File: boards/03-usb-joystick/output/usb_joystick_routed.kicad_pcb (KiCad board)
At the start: 2 copper layers, 80 x 60 mm, 19 parts, among them J1 USB-C, J2 Joystick, SW1 Button, SW2 Button, SW3 Button, SW4 Button, U1 MCU, Y1 16MHz

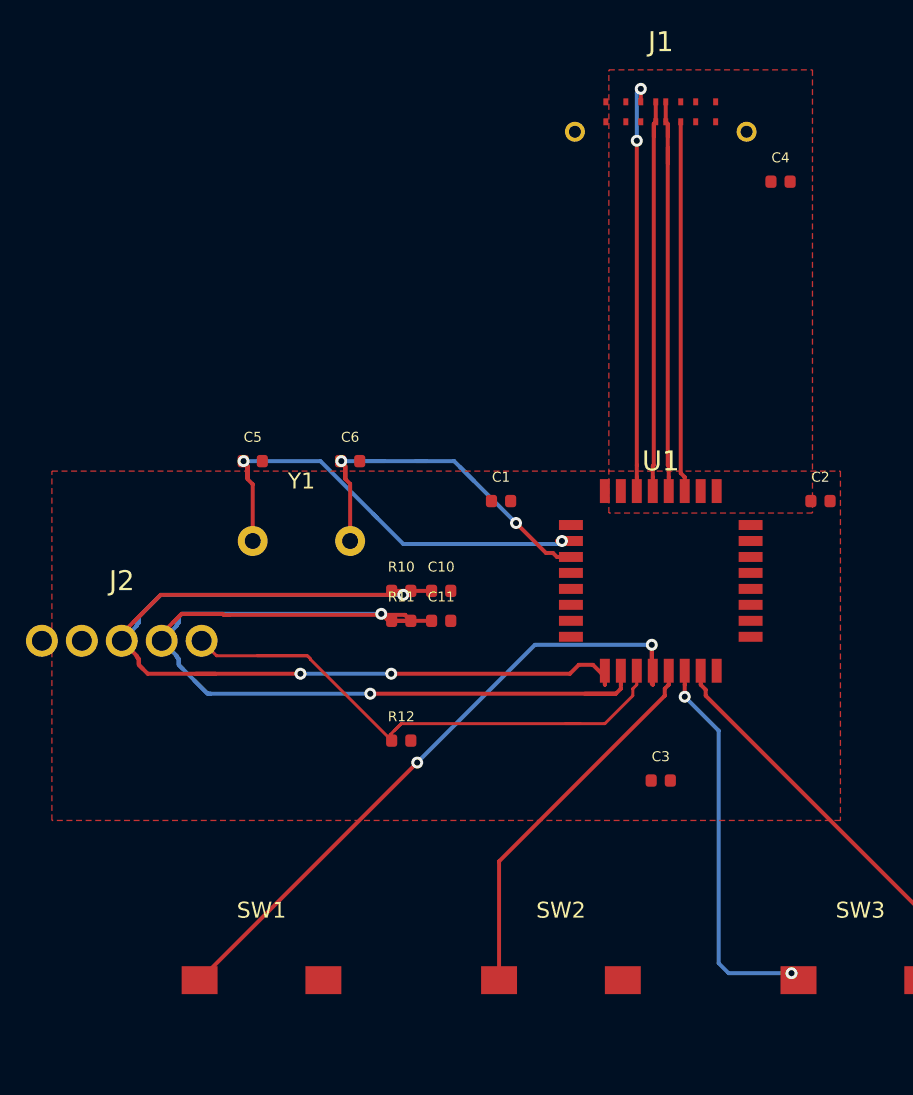
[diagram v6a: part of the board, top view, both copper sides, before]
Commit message: fix(boards/03): restore refill-only routed PCB from bundle — undo in-place re-route clobber
The committed usb_joystick_routed.kicad_pcb at the previous head was a
re-clobbered re-route (570 segments, 257/245 multiset diff vs main) — an
in-place test/demo run overwrote the artifact AFTER the correct refill
(same failure class as issue #3580). The correct refill-only artifact
survived inside manufacturing/kicad_project.zip; this commit restores the
standalone file from that zip (now byte-identical to the bundle-embedded
PCB, sha256 b793b9b4).

Independently re-verified vs origin/main:
- 582 segments, (start,end,width,layer,net) multiset identical (0/0 diff)
- 15 vias identical, 19 footprints, 4 zone outlines unchanged
- filled_polygon data is the only substantive diff (7/10 polygons regenerated)
- kct check --mfr jlcpcb-tier1 --only segment_zone --errors-only: 0
- full kct check --mfr jlcpcb-tier1: 0 errors / 16 warnings
- scripts/ci/check_routed_drc.py strict gate: OK — 0 errors

No bundle changes needed: kicad_project.zip sha256 already matches
manifest.json (32827137…, 83827 bytes).

Co-Authored-By: Claude Opus 4.7 <noreply@anthropic.com>
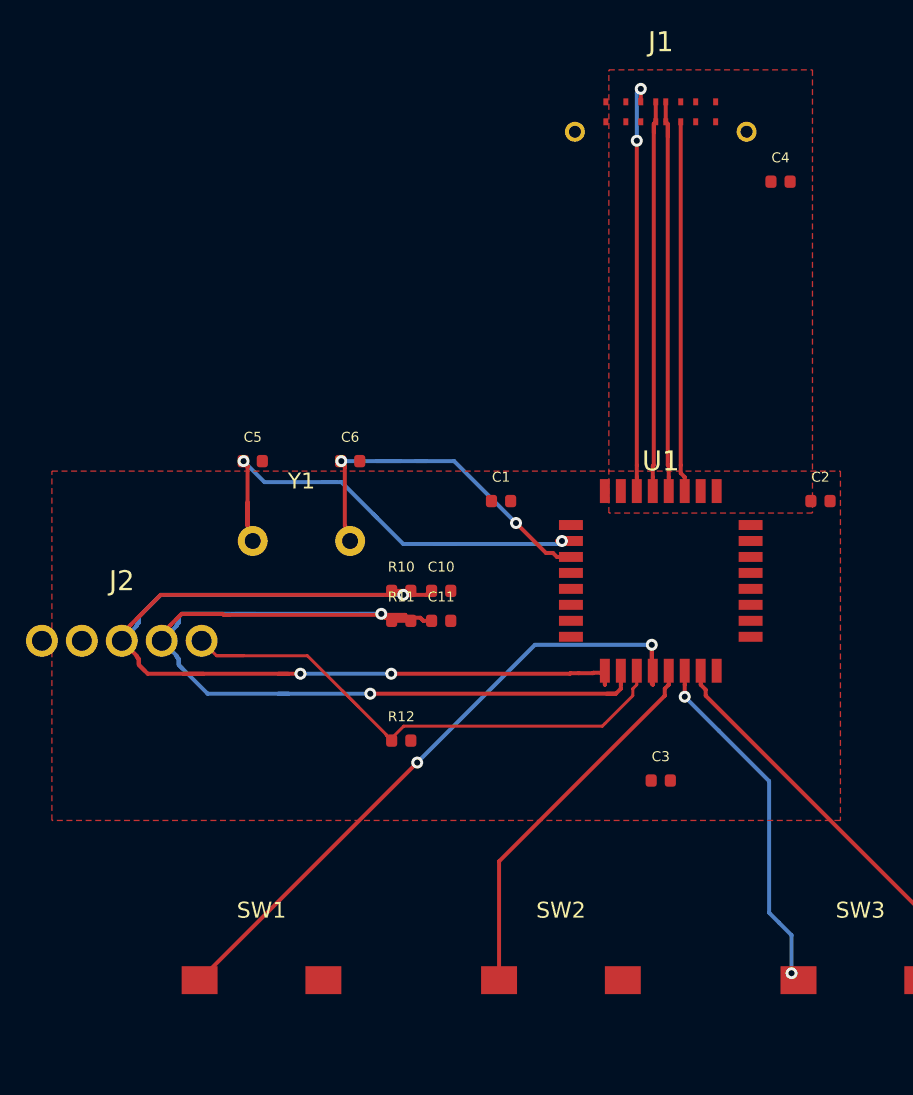
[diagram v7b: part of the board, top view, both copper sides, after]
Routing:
- net BTN3: track 19.7 -> 17.9 mm

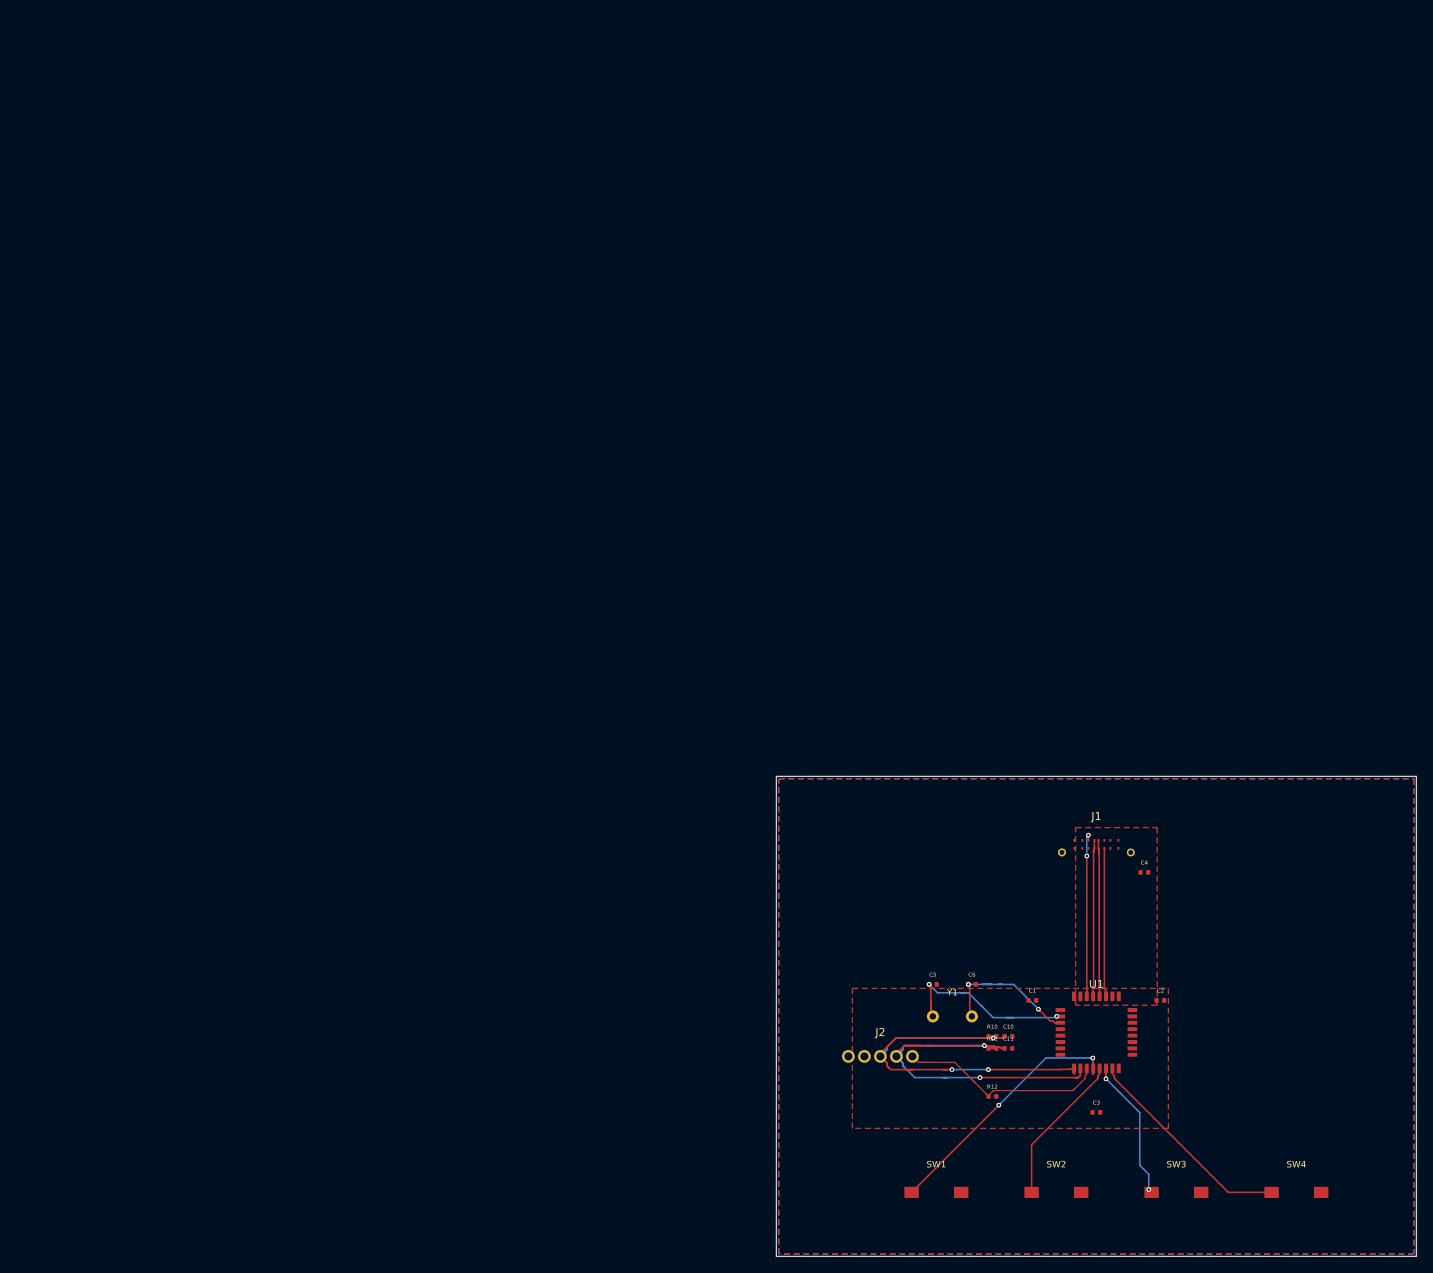
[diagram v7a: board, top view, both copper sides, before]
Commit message: feat(pcb): add page_fit to size sheet to board + center, apply to all boards
Add PCB.page_fit(margin=5.0) which rewrites the (paper ...) node to a tight
(paper "User" W H) sized to the Edge.Cuts bbox plus a uniform margin and
translates every board item (footprints, segments, vias, zones incl.
filled_polygons, gr_* graphics, text) so the board is centered with that
margin. Pure geometric translate — relative geometry, routing and DRC
validity are preserved, no re-route needed.

Expose it as `kct pcb page-fit <pcb> [-o out] [--margin] [--dry-run]` and
wire a PAGE_FIT build step (after stitch, before verify/export) so future
boards are centered too. Apply page_fit to all demo boards (00-07 +
external/softstart), both routed and unrouted PCBs, so the committed
layouts fill + center the KiCanvas viewer instead of sitting tiny in an A4
page. Boards 00/01 stay DRC-clean (0 errors); no board's DRC count changed.

Co-Authored-By: Claude Opus 4.7 <noreply@anthropic.com>
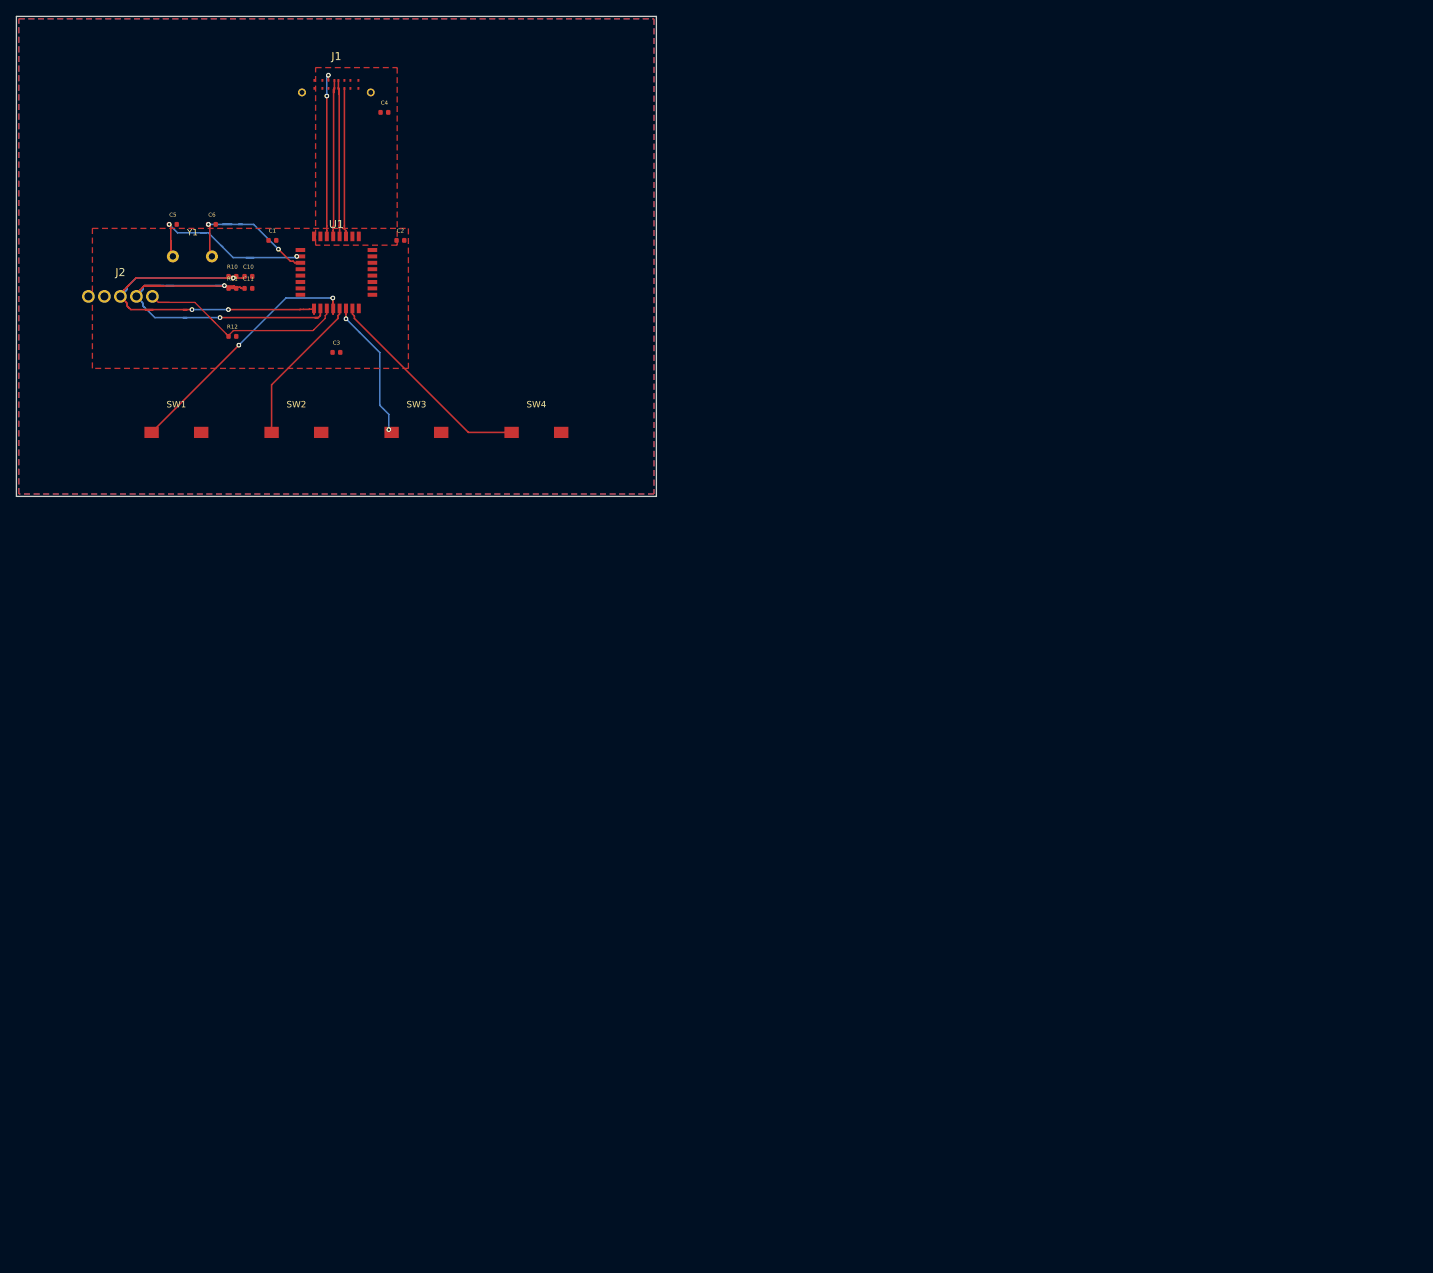
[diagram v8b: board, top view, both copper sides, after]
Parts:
- moved C1 134.4 mm to (37.0, 33.0)
- moved C10 134.4 mm to (34.0, 37.5)
- moved C11 134.4 mm to (34.0, 39.0)
- moved C2 134.4 mm to (53.0, 33.0)
- moved C3 134.4 mm to (45.0, 47.0)
- moved C4 134.4 mm to (51.0, 17.0)
- moved C5 134.4 mm to (24.6, 31.0)
- moved C6 134.4 mm to (29.4, 31.0)
- moved J1 134.4 mm to (45.0, 13.0)
- moved J2 134.4 mm to (18.0, 40.0)
- moved R10 134.4 mm to (32.0, 37.5)
- moved R11 134.4 mm to (32.0, 39.0)
- moved R12 134.4 mm to (32.0, 45.0)
- moved SW1 134.4 mm to (25.0, 57.0)
- moved SW2 134.4 mm to (40.0, 57.0)
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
